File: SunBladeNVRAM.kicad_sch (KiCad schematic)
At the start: 7 parts, among them J1 Conn_01x14_Pin, J2 Conn_01x14_Pin, J3 Conn_01x02_Pin, J4 Conn_01x02_Pin, U1 M48T59Y-70MH1, Y1 32.768 kHz

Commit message: assign footprints
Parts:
- J1, J2, Y1: footprint (none) -> Connector_PinHeader_2.54mm:PinHeader_1x14_P2.54mm_Vertical
- J3, J4: footprint (none) -> Connector_PinHeader_2.54mm:PinHeader_1x02_P2.54mm_Vertical
- U1: footprint MODULE -> Package_SO:SOIC-28W_7.5x17.9mm_P1.27mm
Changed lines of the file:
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@@
 			)
 		)
-		(property "Footprint" ""
+		(property "Footprint" "Connector_PinHeader_2.54mm:PinHeader_1x14_P2.54mm_Vertical"
 			(at 102.87 132.08 0)
 			(effects
@@
 			)
 		)
-		(property "Footprint" ""
+		(property "Footprint" "Connector_PinHeader_2.54mm:PinHeader_1x14_P2.54mm_Vertical"
 			(at 78.74 90.17 0)
 			(effects
@@
 			)
 		)
-		(property "Footprint" ""
+		(property "Footprint" "Connector_PinHeader_2.54mm:PinHeader_1x14_P2.54mm_Vertical"
 			(at 157.48 90.17 0)
 			(effects
@@
 			)
 		)
-		(property "Footprint" ""
+		(property "Footprint" "Connector_PinHeader_2.54mm:PinHeader_1x02_P2.54mm_Vertical"
 			(at 101.6 146.05 0)
 			(effects
@@
 			)
 		)
-		(property "Footprint" ""
+		(property "Footprint" "Connector_PinHeader_2.54mm:PinHeader_1x02_P2.54mm_Vertical"
 			(at 134.62 146.05 0)
 			(effects
@@
 			)
 		)
-		(property "Footprint" "MODULE"
+		(property "Footprint" "Package_SO:SOIC-28W_7.5x17.9mm_P1.27mm"
 			(at 118.11 91.44 0)
 			(effects

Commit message: add project footprint lib for battery holder
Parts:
- BT1: footprint BU1632SM-JJ-GTR:BAT_BU1632SM-JJ-GTR -> SunBladeNVRAM:BAT_BU1632SM-JJ-GTR
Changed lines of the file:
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@@
 			)
 		)
-		(property "Footprint" "BU1632SM-JJ-GTR:BAT_BU1632SM-JJ-GTR"
+		(property "Footprint" "SunBladeNVRAM:BAT_BU1632SM-JJ-GTR"
 			(at 135.89 132.08 0)
 			(effects

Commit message: fix watch crystal footprint assignment
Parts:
- Y1: footprint Connector_PinHeader_2.54mm:PinHeader_1x14_P2.54mm_Vertical -> Crystal:Crystal_C38-LF_D3.0mm_L8.0mm_Horizontal
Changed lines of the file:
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@@
 			)
 		)
-		(property "Footprint" "Connector_PinHeader_2.54mm:PinHeader_1x14_P2.54mm_Vertical"
+		(property "Footprint" "Crystal:Crystal_C38-LF_D3.0mm_L8.0mm_Horizontal"
 			(at 102.87 132.08 0)
 			(effects

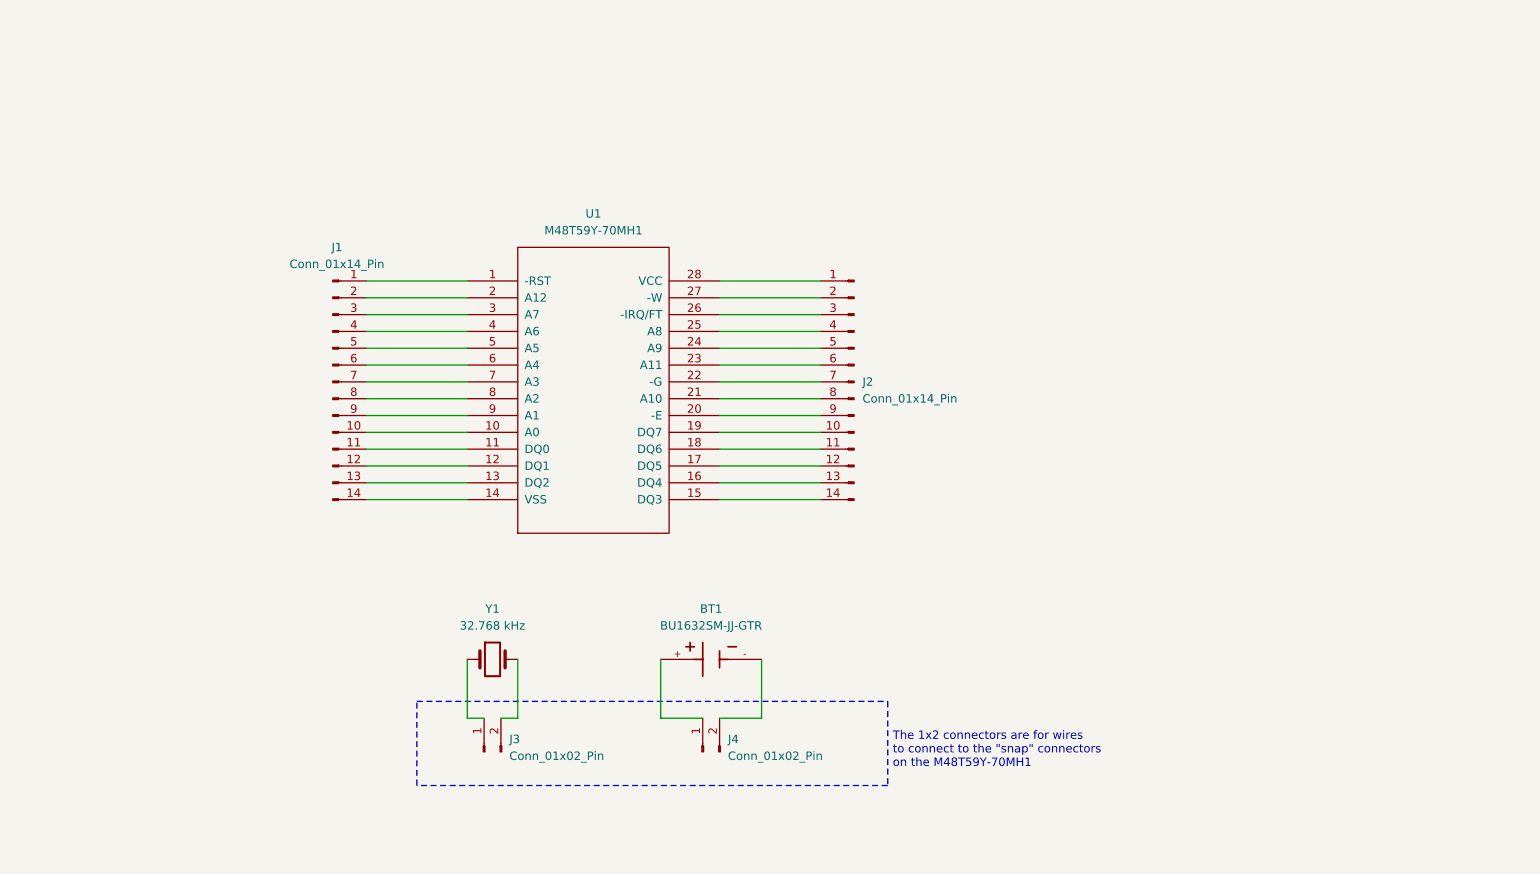
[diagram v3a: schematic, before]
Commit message: put battery on stacked "hat" PCB
There's not enough room for all of the components
otherwise if we want to fit in the area of a standard
DIP28 part.
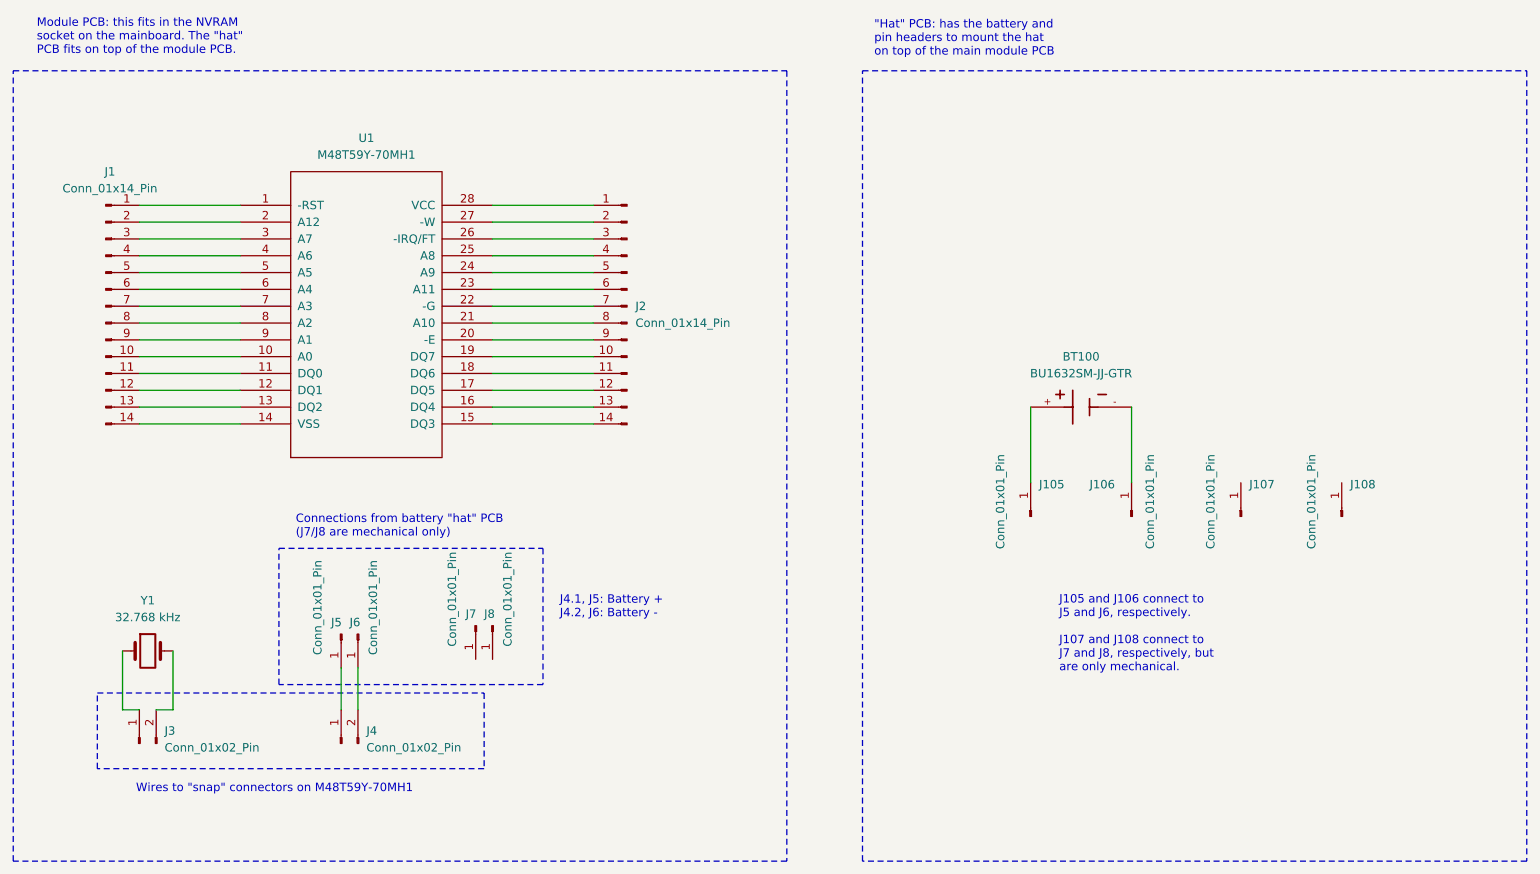
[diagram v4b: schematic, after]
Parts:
- added J105, J106, J107, J108, J5, J6, J7, J8: Conn_01x01_Pin, symbol Connector:Conn_01x01_Pin
- renumbered BT1 to BT100
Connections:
- net at BT100.+: now also J105.1 (Pin_1); no longer J4.1 (Pin_1)
- net at BT100.-: now also J106.1 (Pin_1); no longer J4.2 (Pin_2)
- new net: J4.2 (Pin_2), J6.1 (Pin_1)
- new net: J4.1 (Pin_1), J5.1 (Pin_1)
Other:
- note added: ""Hat" PCB: has the battery and pin headers to mount the hat on top of the main module PCB"
- note added: "Connections from battery "hat" PCB (J7/J8 are mechanical only)"
- note added: "J105 and J106 connect to J5 and J6, respectively. J107 and J108 connect to J7 and J8, respectively, but are only mechanical."
- note added: "J4.1, J5: Battery + J4.2, J6: Battery -"
- note added: "Module PCB: this fits in the NVRAM socket on the mainboard. The "hat" PCB fits on top of the module PCB."
- note added: "Wires to "snap" connectors on M48T59Y-70MH1"
- note removed: "The 1x2 connectors are for wires to connect to the "snap" connectors on the M48T59Y-70MH1"
- moved on the sheet: BT100, J1, J2, J3, J4, U1, Y1

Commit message: assign footprints for single pin headers
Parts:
- J105, J106, J107, J108, J5, J6, J7, J8: footprint (none) -> Connector_PinHeader_2.54mm:PinHeader_1x01_P2.54mm_Vertical
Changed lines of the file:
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@@
 			)
 		)
-		(property "Footprint" ""
+		(property "Footprint" "Connector_PinHeader_2.54mm:PinHeader_1x01_P2.54mm_Vertical"
 			(at 215.9 110.49 0)
 			(effects
@@
 			)
 		)
-		(property "Footprint" ""
+		(property "Footprint" "Connector_PinHeader_2.54mm:PinHeader_1x01_P2.54mm_Vertical"
 			(at 231.14 110.49 0)
 			(effects
@@
 			)
 		)
-		(property "Footprint" ""
+		(property "Footprint" "Connector_PinHeader_2.54mm:PinHeader_1x01_P2.54mm_Vertical"
 			(at 82.55 128.27 0)
 			(effects
@@
 			)
 		)
-		(property "Footprint" ""
+		(property "Footprint" "Connector_PinHeader_2.54mm:PinHeader_1x01_P2.54mm_Vertical"
 			(at 199.39 110.49 0)
 			(effects
@@
 			)
 		)
-		(property "Footprint" ""
+		(property "Footprint" "Connector_PinHeader_2.54mm:PinHeader_1x01_P2.54mm_Vertical"
 			(at 100.33 127 0)
 			(effects
@@
 			)
 		)
-		(property "Footprint" ""
+		(property "Footprint" "Connector_PinHeader_2.54mm:PinHeader_1x01_P2.54mm_Vertical"
 			(at 102.87 127 0)
 			(effects
@@
 			)
 		)
-		(property "Footprint" ""
+		(property "Footprint" "Connector_PinHeader_2.54mm:PinHeader_1x01_P2.54mm_Vertical"
 			(at 184.15 110.49 0)
 			(effects
@@
 			)
 		)
-		(property "Footprint" ""
+		(property "Footprint" "Connector_PinHeader_2.54mm:PinHeader_1x01_P2.54mm_Vertical"
 			(at 80.01 128.27 0)
 			(effects
